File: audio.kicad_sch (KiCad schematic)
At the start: 14 parts, among them U1 NCS603

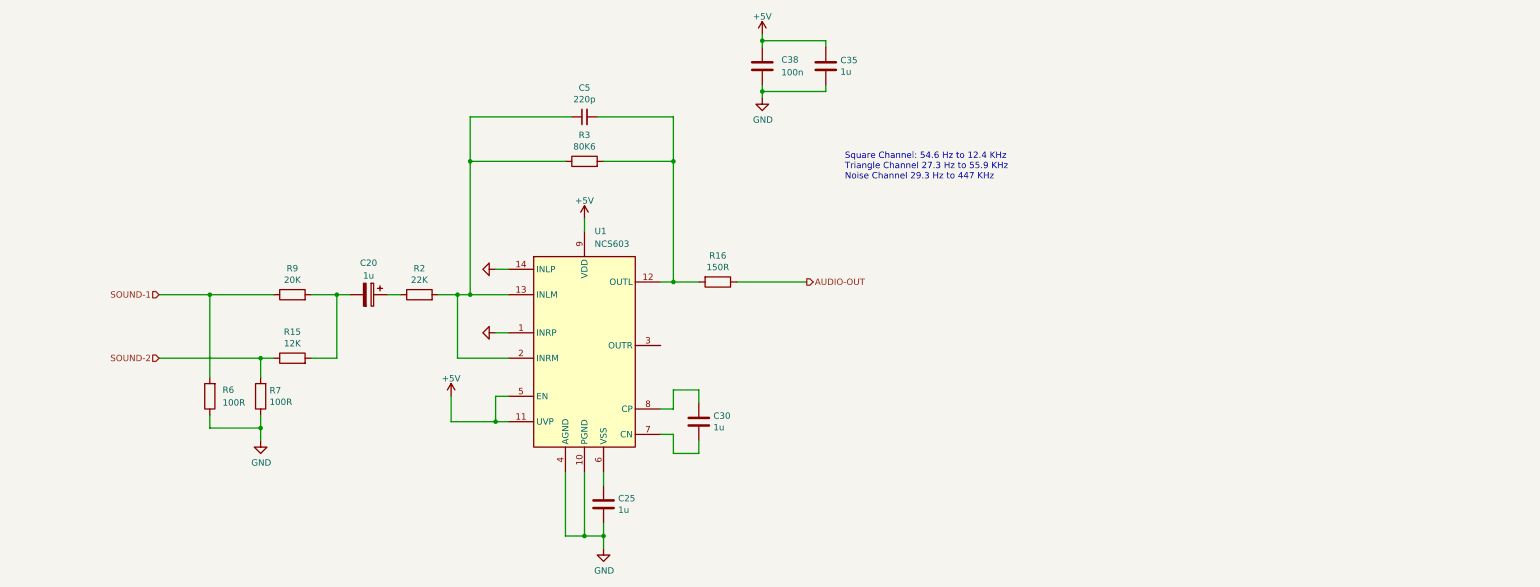
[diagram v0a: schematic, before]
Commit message: rev2 sent to fab
Added CHR RAM.
Changed board to 4 layers (was 2 layers).
Changed passives to 0603 (was 0402)
Fixed CIRAM-A10 not being hooked up
Fixed PPU-A10..A12 being hooked to VRAM but should have been.
Added more silkscreen for easier debugging.
Added filter inductor to 5V from USB-C.
Changed video out to stock (was THS7374)
Changed audio circuit to stock (was headphone amp IC)
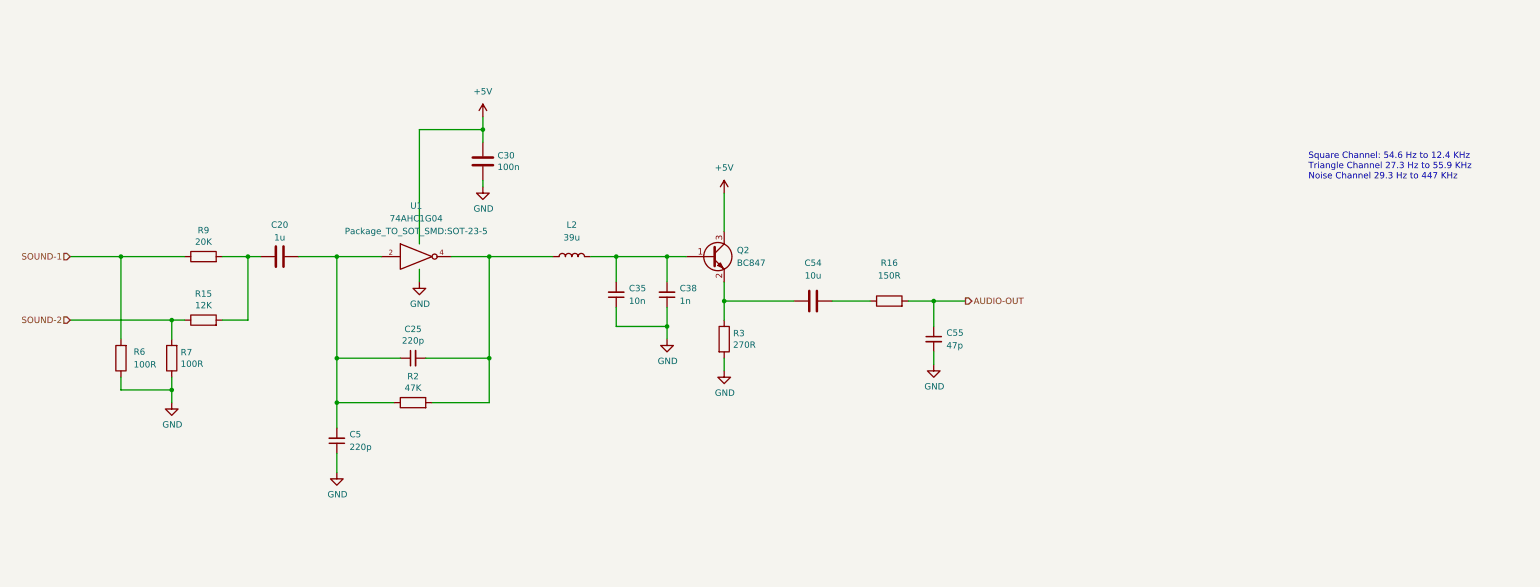
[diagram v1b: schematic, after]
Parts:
- removed C25, C35: 1u, Capacitor_SMD:C_0402_1005Metric, symbol Device:C
- removed C38: 100n, Capacitor_SMD:C_0402_1005Metric, symbol Device:C
- removed U1: NCS603, Package_SO:TSSOP-14_4.4x5mm_P0.65mm, symbol 00Custom:NCS603
- added C25: 220p, Capacitor_SMD:C_0603_1608Metric_Pad1.08x0.95mm_HandSolder, symbol Device:C_Small
- added C35: 10n, Capacitor_SMD:C_0603_1608Metric_Pad1.08x0.95mm_HandSolder, symbol Device:C_Small
- added C38: 1n, Capacitor_SMD:C_0603_1608Metric_Pad1.08x0.95mm_HandSolder, symbol Device:C_Small
- added C54: 10u, Capacitor_SMD:C_1206_3216Metric_Pad1.33x1.80mm_HandSolder, symbol Device:C
- added C55: 47p, Capacitor_SMD:C_0603_1608Metric_Pad1.08x0.95mm_HandSolder, symbol Device:C_Small
- added L2: 39u, Inductor_SMD:L_0805_2012Metric_Pad1.05x1.20mm_HandSolder, symbol Device:L
- added Q2: BC847, Package_TO_SOT_SMD:SOT-23_Handsoldering, symbol Transistor_BJT:BC847
- added U1: 74AHC1G04, Package_TO_SOT_SMD:SOT-23-5, symbol 74xGxx:74AHC1G04
- C20: footprint Capacitor_SMD:C_0402_1005Metric -> Capacitor_SMD:C_0603_1608Metric_Pad1.08x0.95mm_HandSolder; symbol Device:C_Polarized -> Device:C; Digikey 490-3890-2-ND -> (none); MPN GRM155R61A105KE15D -> (none); Size 0402 -> (none)
- C30: value 1u -> 100n; footprint Capacitor_SMD:C_0402_1005Metric -> Capacitor_SMD:C_0603_1608Metric_Pad1.08x0.95mm_HandSolder; Digikey 490-3890-2-ND -> (none); MPN GRM155R61A105KE15D -> (none); Size 0402 -> (none)
- C5: footprint Capacitor_SMD:C_0402_1005Metric -> Capacitor_SMD:C_0603_1608Metric_Pad1.08x0.95mm_HandSolder; Digikey 1276-1059-1-ND -> (none); MPN CL05C221JB5NNNC -> (none)
- R15: footprint Resistor_SMD:R_0402_1005Metric -> Resistor_SMD:R_0603_1608Metric_Pad0.98x0.95mm_HandSolder; Digikey 13-RC0402FR-1312KLCT-ND -> (none); MPN RC0402FR-1312KL -> (none)
- R16: footprint Resistor_SMD:R_0603_1608Metric -> Resistor_SMD:R_0603_1608Metric_Pad0.98x0.95mm_HandSolder; Digikey 311-150HRCT-ND -> (none); MPN RC0603FR-07150RL -> (none)
- R2: value 22K -> 47K; footprint Resistor_SMD:R_0402_1005Metric -> Resistor_SMD:R_0603_1608Metric_Pad0.98x0.95mm_HandSolder; Digikey 311-22.0KLRCT-ND -> (none); MPN RC0402FR-0722KL -> (none)
- R3: value 80K6 -> 270R; footprint Resistor_SMD:R_0402_1005Metric -> Resistor_SMD:R_0603_1608Metric_Pad0.98x0.95mm_HandSolder; Digikey 311-80.6KLRCT-ND -> (none); MPN RC0402FR-0780K6L -> (none)
- R6, R7: footprint Resistor_SMD:R_0402_1005Metric -> Resistor_SMD:R_0603_1608Metric_Pad0.98x0.95mm_HandSolder; Digikey P100LCT-ND -> (none); MPN ERJ-2RKF1000X -> (none)
- R9: footprint Resistor_SMD:R_0402_1005Metric -> Resistor_SMD:R_0603_1608Metric_Pad0.98x0.95mm_HandSolder; Digikey RR05P20.0KDCT-ND -> (none); MPN RR0510P-203-D -> (none); QOH 1000 -> (none)
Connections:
- net +5V: now also C30.2, Q2.3 (C), U1.5 (VCC)
- net AUDIO-OUT: now also R16.2, C55.1; no longer R16.1
- net GND: now also C30.1, C5.1, R3.2, C35.1, C38.1, C55.2, U1.3 (GND)
- net at C20.1, R2.1: now also C5.2, C25.1, U1.2
- new net: C35.2, C38.2, L2.2, Q2.1 (B)
- new net: C54.1, Q2.2 (E), R3.1
- new net: C25.2, L2.1, R2.2, U1.4
- new net: C54.2, R16.1
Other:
- moved on the sheet: R15, R6, R7, R9

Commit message: filled out BOM
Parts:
- C20: Digikey (none) -> 1276-1102-1-ND; MPN (none) -> CL10A105KA8NNNC
- C25, C5: Digikey (none) -> 399-C0603C221J5GAC7867CT-ND; MPN (none) -> C0603C221J5GAC7867
- C30: Digikey (none) -> 1276-CL10B104KB8WPNDCT-ND; MPN (none) -> CL10B104KB8WPND
- C35: Digikey (none) -> 399-C0603C103J3GAC7867CT-ND; MPN (none) -> C0603C103J3GAC7867
- C38: Digikey (none) -> 399-C0603C102J5GAC7867CT-ND; MPN (none) -> C0603C102J5GAC7867
- C54: Digikey (none) -> 1276-1075-1-ND; MPN (none) -> CL31A106KAHNNNE
- C55: Digikey (none) -> 399-C0603C470K5GAC7867CT-ND; MPN (none) -> C0603C470K5GAC7867
- Q2: Digikey (none) -> BC847CLT1GOSCT-ND; MPN (none) -> BC847CLT1G
- R15: Digikey (none) -> RMCF0603FT12K0CT-ND; MPN (none) -> RMCF0603FT12K0
- R16: Digikey (none) -> RNCP0603FTD150RCT-ND; MPN (none) -> RNCP0603FTD150R
- R2: Digikey (none) -> RMCF0603FT47K0CT-ND; MPN (none) -> RMCF0603FT47K0
- R3: Digikey (none) -> RMCF0603FT270RCT-ND; MPN (none) -> RMCF0603FT270R
- R6, R7: Digikey (none) -> RMCF0603FT100RCT-ND; MPN (none) -> RMCF0603FT100R
- R9: Digikey (none) -> RMCF0603FT20K0CT-ND; MPN (none) -> RMCF0603FT20K0
